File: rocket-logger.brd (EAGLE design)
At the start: 58.5 x 62 mm, 71 parts, among them IC1 CC430F513X, U1 MAX1555, X1 0896BM15A0001, X2 USB-MICROB, X3 SMA-142-0701-801/806

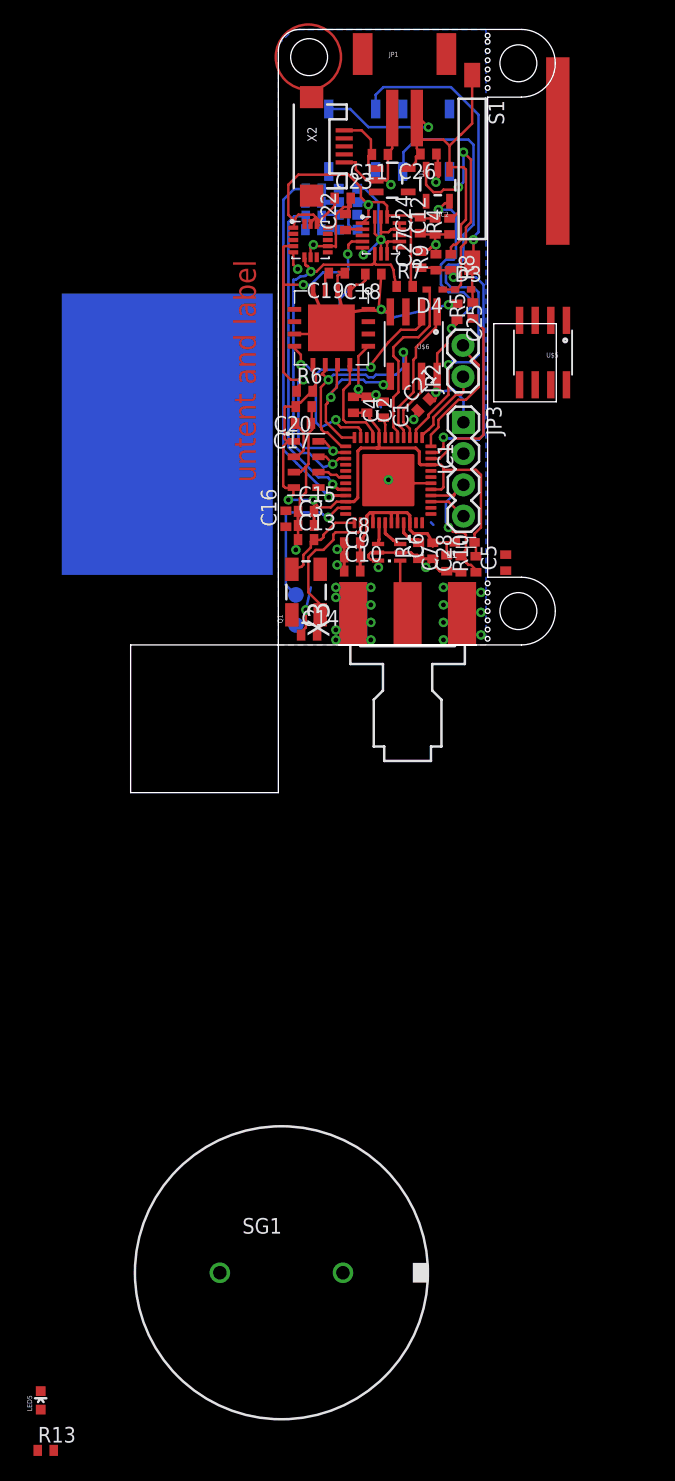
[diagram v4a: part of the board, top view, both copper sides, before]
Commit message: added diodes on power path
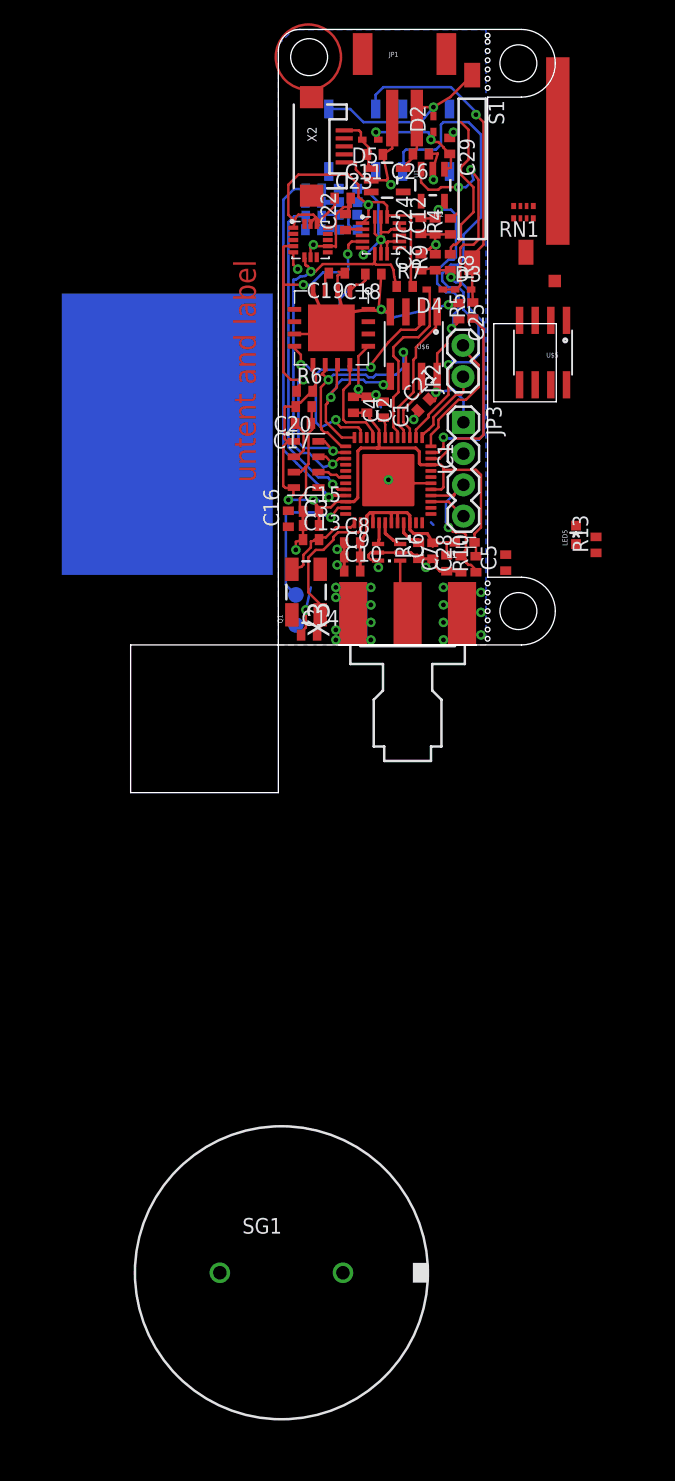
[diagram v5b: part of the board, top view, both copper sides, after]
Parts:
- added C29: (no value), resistor:C0402
- added D2, D5: (no value), diode:SOD523
- added RN1: (no value), resistor-dil:4X0402ARV341
- moved R13 86.1 mm to (25.8, 8.13), turned to 90 degrees
- moved LED5 82.7 mm to (24.2, 8.94)
- moved C26 0.61 mm to (11.6, 39.9)
- moved IC2 0.41 mm to (12.5, 37.3)
- moved C13 0.41 mm to (2.66, 8.56)
- moved C15 0.41 mm to (2.66, 10.9)
- moved C3 0.41 mm to (2.66, 9.70)
- moved C11 0.41 mm to (7.84, 39.8)
- moved U1 0.41 mm to (8.84, 37.8)
- moved C16 0.20 mm to (0.81, 10.2)
- moved C27 0.20 mm to (11.6, 31.1)
- moved C25 0.16 mm to (14.7, 27.1)
- moved C24 0.07 mm to (11.6, 34.0)
- moved R4 0.05 mm to (14.0, 34.0)
- moved R9 0.05 mm to (12.8, 31.1)
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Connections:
- new net N$30: C29.2, D2.C, D5.C, IC2.1
- net GND: now also C29.1
- net N$1: now also D5.A
- net N$2: now also D2.A; no longer IC2.1
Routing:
- net N$30: track 0.00 -> 10.0 mm, vias 0 -> 2
- net N$28: track 38.5 -> 41.5 mm
- net GND: track 134.1 -> 136.8 mm, vias 34 -> 35
- net N$25: track 23.3 -> 22.2 mm
- net +3V3: track 119.6 -> 118.5 mm
- net VBAT: track 24.1 -> 23.2 mm
- net N$6: track 7.46 -> 8.26 mm
- net N$24: track 27.1 -> 27.7 mm
- net N$2: track 34.9 -> 34.4 mm

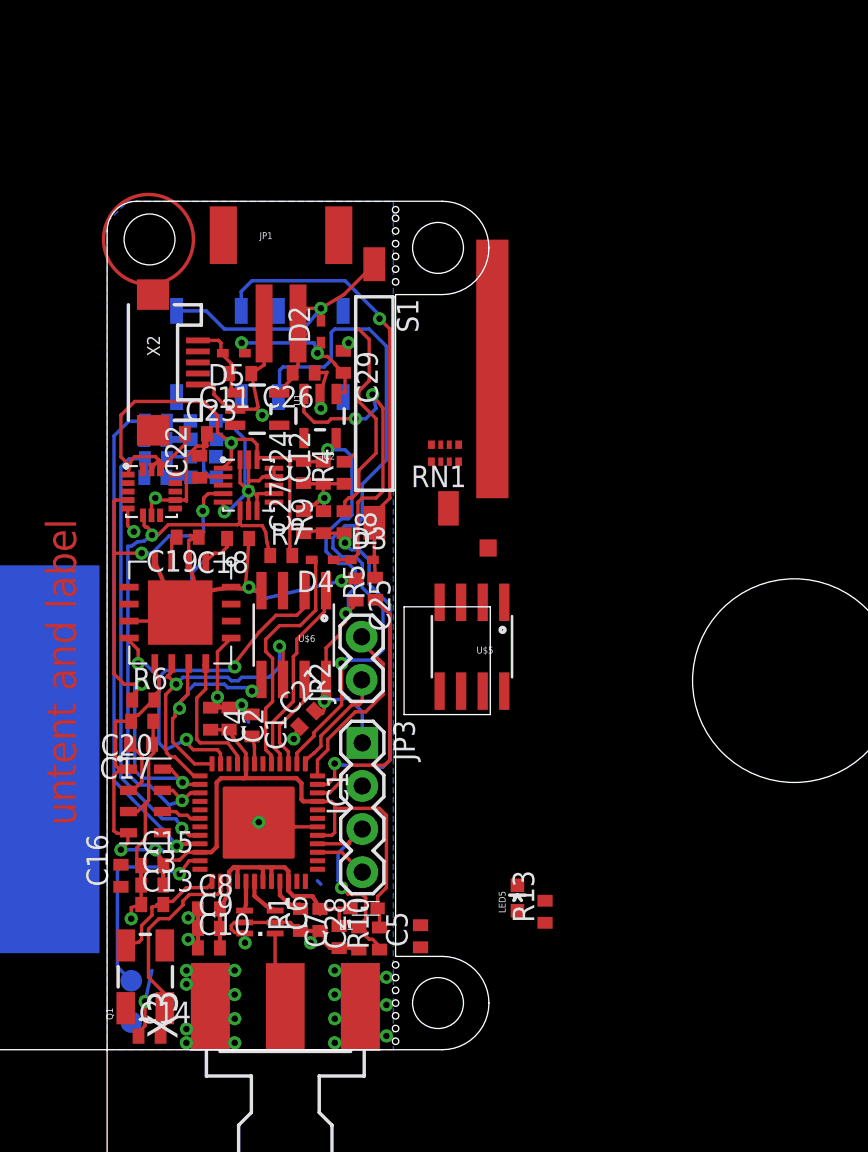
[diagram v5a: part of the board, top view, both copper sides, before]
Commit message: switched to smaller jst connector and done routing
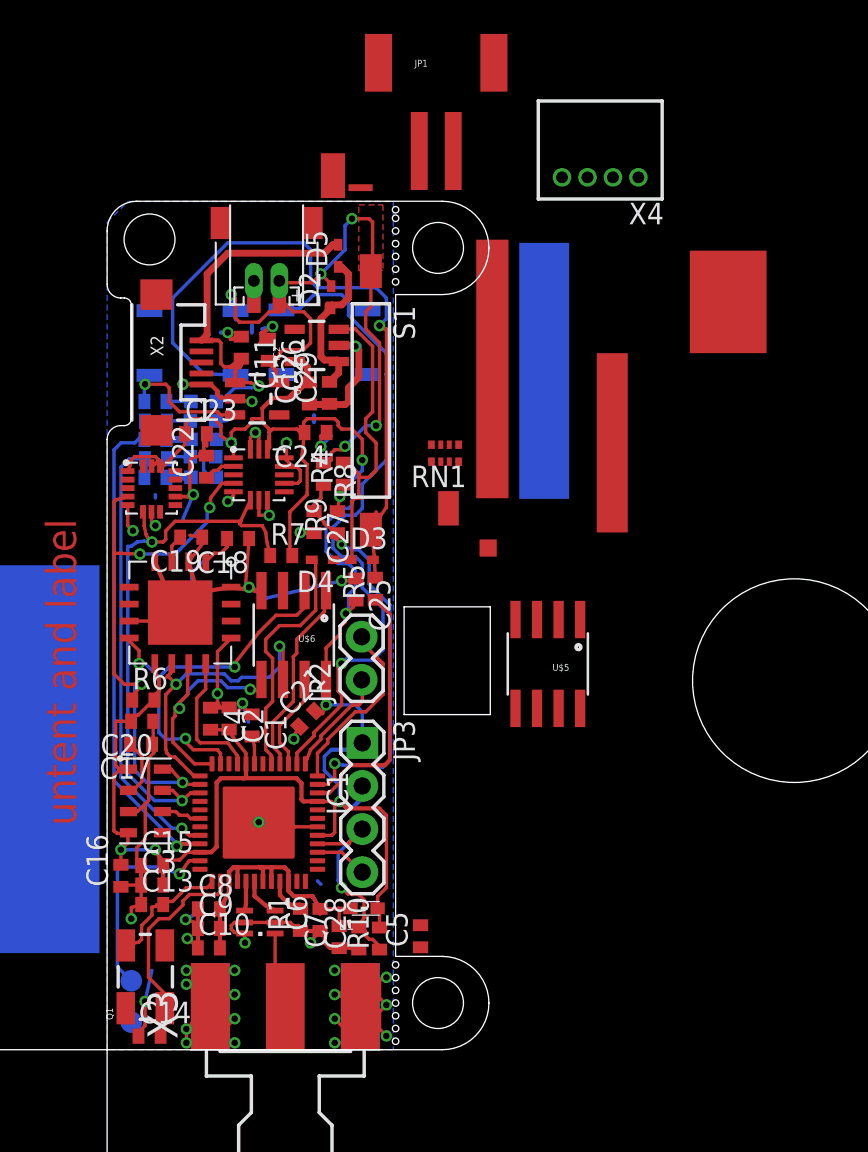
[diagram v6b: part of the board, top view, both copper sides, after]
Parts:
- added U$7: JST-ZR-2, Mine:JST-ZR-2
- added U$8: JST-ZR-2SMD, Mine:JST-ZR-2-SMD
- added X4: S4B-ZR, con-jst:S4B-ZR
- moved R13 37.8 mm to (2.84, 38.2), flipped to the bottom, turned to 180 degrees
- moved LED5 34.6 mm to (5.69, 38.2), flipped to the bottom, turned to 270 degrees
- moved JP1 13.7 mm to (19.4, 56.7)
- moved D5 8.34 mm to (13.6, 46.7), turned to 90 degrees
- moved C12 4.74 mm to (11.9, 38.7)
- moved U$5 4.58 mm to (26.0, 22.7)
- moved IC2 4.17 mm to (12.3, 41.5), turned to 90 degrees
- moved R8 3.10 mm to (12.8, 33.9)
- moved C26 2.49 mm to (9.50, 41.2), turned to 270 degrees
- moved C24 2.43 mm to (12.3, 36.4), turned to 180 degrees
- moved D2 2.12 mm to (13.2, 44.3)
- moved C29 2.00 mm to (13.1, 38.7), turned to 90 degrees
- moved C11 1.53 mm to (7.90, 41.4), turned to 270 degrees
- moved S2 1.16 mm to (5.03, 41.7), turned to 0 degrees
- moved S4 1.06 mm to (12.8, 41.7), turned to 180 degrees
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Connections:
- net GND: now also S4.1, U$7.2, U$8.2
- net N$2: now also U$7.1, U$8.1
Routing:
- net N$1: track 5.33 -> 23.3 mm, vias 0 -> 1
- net N$24: track 27.7 -> 43.1 mm
- net GND: track 136.8 -> 150.4 mm, vias 35 -> 42
- net +3V3: track 118.5 -> 128.8 mm, vias 6 -> 7
- net N$2: track 34.4 -> 43.2 mm, vias 1 -> 5
- net N$10: track 0.00 -> 7.57 mm, vias 0 -> 1
- net N$25: track 22.2 -> 19.3 mm, vias 2 -> 0
- net N$28: track 41.5 -> 39.4 mm
- net VBAT: track 23.2 -> 25.2 mm
- net SDA: track 32.6 -> 34.3 mm
- net N$18: track 0.00 -> 1.44 mm
- net N$19: track 1.41 -> 2.21 mm
- net MISO: track 23.7 -> 22.9 mm
- net N$30: track 10.0 -> 9.67 mm, vias 2 -> 0
- added copper zone on layer 1, net N$2
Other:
- outline, holes or cut-outs redrawn
- board text added: "+"
- board text added: "1"
- board text added: "2"
- board text added: "C"
- board text added: "CHG"
- board text added: "CLR"
- board text added: "GND"
- board text added: "M BREJZA"
- board text added: "MEM"
- board text added: "MI"
- board text added: "MO"
- board text added: "PWR"
- board text added: "ROCKET LOGGER"
- board text added: "RST"
- board text added: "RX"
- board text added: "SC"
- board text added: "SD"
- board text added: "SUSF"
- board text added: "TST"
- board text added: "TX"
- board text added: "V1 NOV 13"
- board text added: "VCC"
- board text removed: "CLR MEM"
- board text removed: "GRN"
- board text removed: "RED"
- board text removed: "YEL"

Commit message: some more routing
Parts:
- moved JP1 3.33 mm to (17.4, 59.3)
- moved C18 0.21 mm to (7.92, 30.2)
- moved C6 0.10 mm to (12.5, 7.75)
- moved R1 0.10 mm to (11.4, 7.75)
- moved R12 0.05 mm to (2.84, 35.9)
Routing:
- net GND: track 150.4 -> 135.8 mm, vias 42 -> 45
- net AVCC_RF2: track 17.9 -> 20.2 mm
- net N$24: track 43.1 -> 40.9 mm
- net N$28: track 39.4 -> 37.5 mm
- net +3V3: track 128.8 -> 126.9 mm
- net VBAT: track 25.2 -> 23.7 mm
- net N$10: track 7.57 -> 8.91 mm
- net N$1: track 23.3 -> 22.1 mm
- net CS_F: track 12.8 -> 11.7 mm
- net N$2: track 43.2 -> 42.3 mm
- net N$6: track 8.26 -> 7.76 mm
- added copper zone on layer 1, net +3V3
- added copper zone on layer 1, net N$3
- added copper zone on layer 1, net N$31
- added copper zone on layer 1, net N$32
- added copper zone on layer 1, net N$4
- added copper zone on layer 1, net N$8

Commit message: some routing done, changed lipo charger
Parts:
- removed U1: MAX1555, SparkFun:SOT23-5
- added C30: (no value), resistor:C0402
- added R14: (no value), rcl:R0402
- added U2: MCP73831, SparkFun-PowerIC:SOT23-5
- moved C5 7.12 mm to (18.1, 13.8)
- moved C22 1.92 mm to (6.33, 32.5), turned to 270 degrees
- moved U$3 0.64 mm to (9.55, 33.7)
- moved C11 0.64 mm to (7.35, 41.7)
- moved C23 0.45 mm to (5.64, 36.1)
- moved C26 0.45 mm to (9.70, 41.7)
- moved U$1 0.41 mm to (2.62, 32.7)
- moved C12 0.41 mm to (12.3, 38.7)
- moved C29 0.41 mm to (13.5, 38.7)
- moved IC2 0.20 mm to (12.3, 41.7)
- moved C19 0.20 mm to (4.75, 30.2)
- moved R7 0.20 mm to (10.1, 29.1)
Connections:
- new net N$33: R14.1, U2.5
- net +3V3: now also C30.1, U$1.7, U$1.8
- net GND: now also C30.2, R14.2, U2.2; no longer U$1.7, U1.2
- net N$1: now also U2.4; no longer U1.1
- net N$10: now also U2.1; no longer U1.3
- net N$2: now also U2.3; no longer U1.5
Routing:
- net GND: track 135.8 -> 145.1 mm
- net N$33: track 0.00 -> 4.21 mm
- net N$1: track 22.1 -> 25.2 mm
- net +3V3: track 126.9 -> 125.6 mm, vias 7 -> 8
- net N$10: track 8.91 -> 10.2 mm
- net N$2: track 42.3 -> 43.2 mm
- net SCL: track 35.0 -> 35.6 mm
- net SDA: track 34.8 -> 34.1 mm, vias 2 -> 3
